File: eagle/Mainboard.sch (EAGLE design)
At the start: 31 parts, among them IC1 L293D, IC2 TLC272P, IC3 LM1085IT-5.0

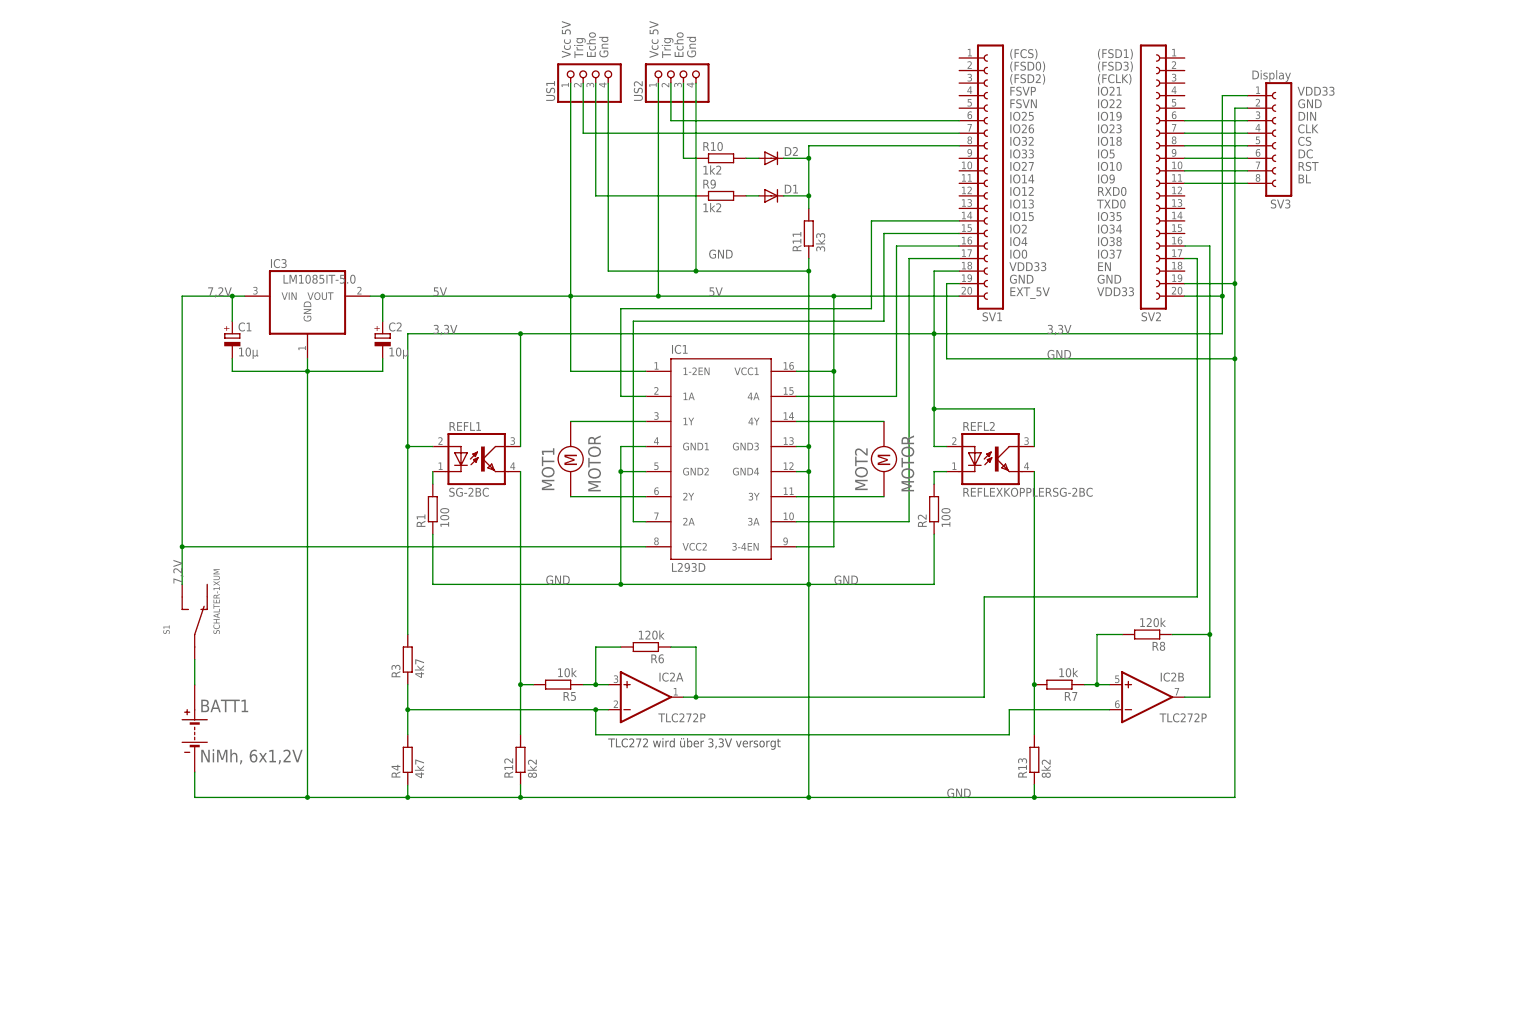
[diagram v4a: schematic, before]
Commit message: Messung Akkuspannung hinzugefügt. SPI-Pins verschoben, damit sie mit SPI3 zusammenpassen
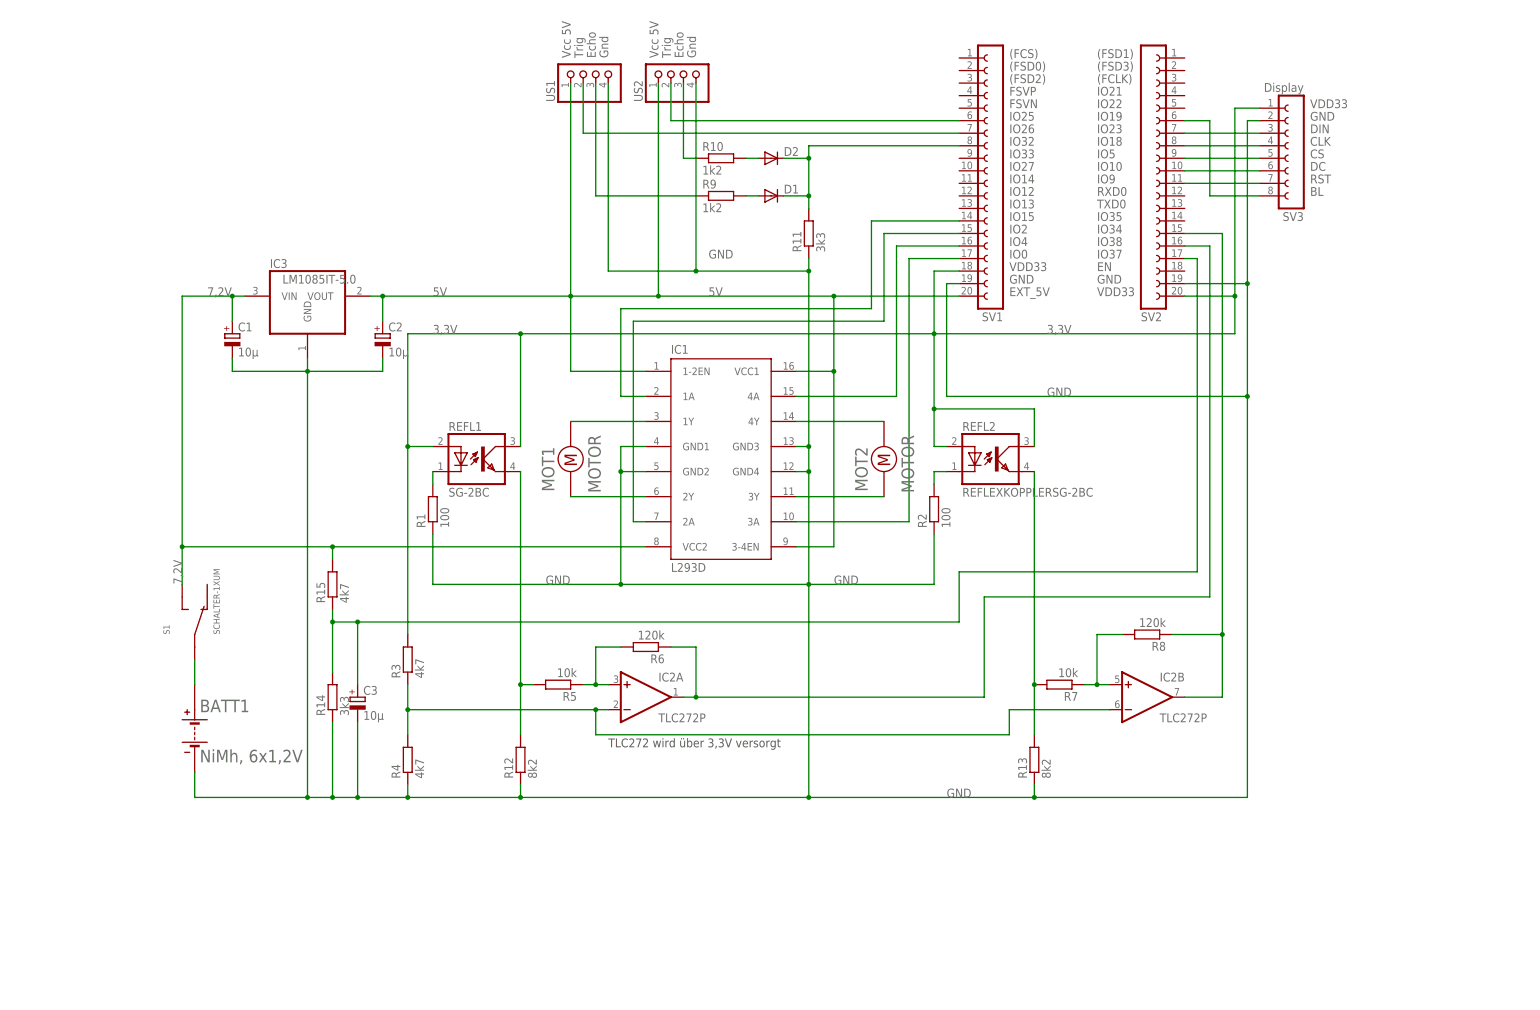
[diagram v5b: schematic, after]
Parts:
- added C3: 10µ, rcl:CPOL-EUE3.5-10
- added R14: 3k3, rcl:R-EU_RDH/15
- added R15: 4k7, rcl:R-EU_RDH/15
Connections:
- removed net N$27: SV2.11, SV3.8
- new net N$20: SV2.6, SV3.8
- new net N$25: C3.+, R14.2, R15.1, SV2.17
- net 7,2V: now also R15.2
- net GND: now also C3.-, R14.1
- net N$11: now also SV2.8; no longer SV2.7
- net N$16: now also SV2.9; no longer SV2.8
- net N$17: now also SV2.10; no longer SV2.9
- net N$18: now also SV2.11; no longer SV2.10
- net N$21: now also SV2.16; no longer SV2.17
- net N$28: now also SV2.15; no longer SV2.16
- net N$8: now also SV2.7; no longer SV2.6
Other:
- moved on the sheet: SV3

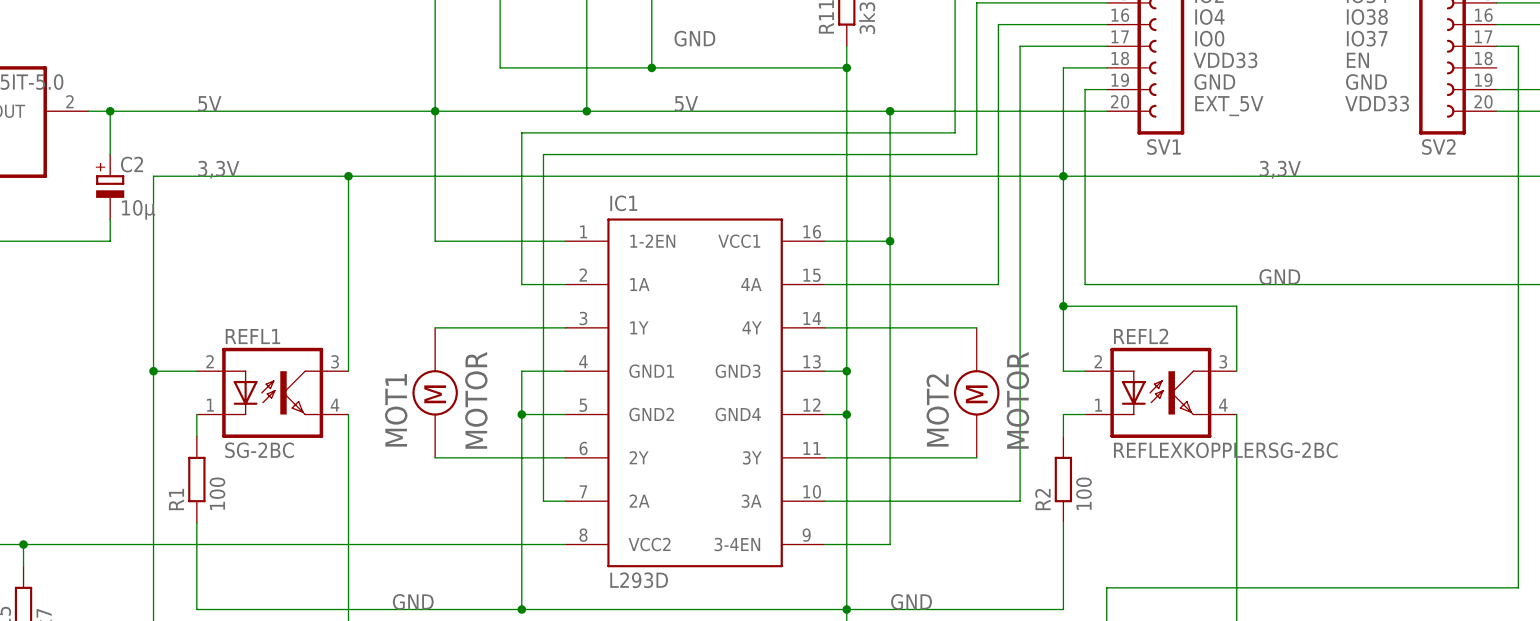
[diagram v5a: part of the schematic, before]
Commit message: Sketch für Mainboard hinzugefügt
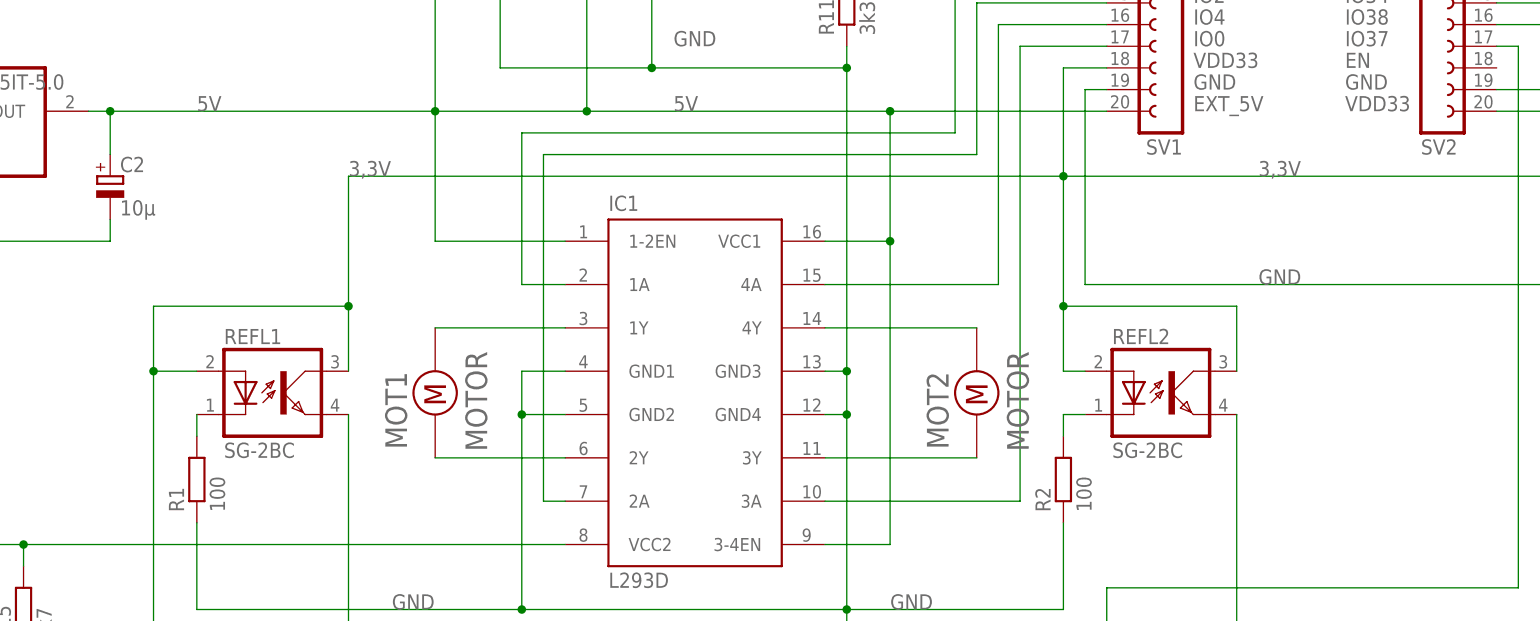
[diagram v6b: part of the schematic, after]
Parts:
- REFL2: value REFLEXKOPPLERSG-2BC -> SG-2BC
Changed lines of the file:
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@@
 <part name="IC1" library="st-microelectronics" library_urn="urn:adsk.eagle:library:368" deviceset="L293D" device="" package3d_urn="urn:adsk.eagle:package:26820/1"/>
 <part name="REFL1" library="bs_lib" deviceset="REFLEXKOPPLER" device="SG-2BC" value="SG-2BC"/>
-<part name="REFL2" library="bs_lib" deviceset="REFLEXKOPPLER" device="SG-2BC"/>
+<part name="REFL2" library="bs_lib" deviceset="REFLEXKOPPLER" device="SG-2BC" value="SG-2BC"/>
 <part name="IC2" library="linear" library_urn="urn:adsk.eagle:library:262" deviceset="TLC272" device="P" package3d_urn="urn:adsk.eagle:package:16409/2"/>
 <part name="MOT1" library="bs_lib" deviceset="MOTOR" device=""/>
@@
 <wire x1="208.28" y1="106.68" x2="198.12" y2="106.68" width="0.1524" layer="91"/>
 <pinref part="REFL1" gate="G$1" pin="COL"/>
-<wire x1="63.5" y1="99.06" x2="63.5" y2="76.2" width="0.1524" layer="91"/>
-<wire x1="40.64" y1="99.06" x2="63.5" y2="99.06" width="0.1524" layer="91"/>
+<wire x1="63.5" y1="99.06" x2="63.5" y2="83.82" width="0.1524" layer="91"/>
+<wire x1="63.5" y1="83.82" x2="63.5" y2="76.2" width="0.1524" layer="91"/>
 <wire x1="147.32" y1="99.06" x2="63.5" y2="99.06" width="0.1524" layer="91"/>
 <junction x="147.32" y="99.06"/>
-<junction x="63.5" y="99.06"/>
 <pinref part="REFL2" gate="G$1" pin="A"/>
 <wire x1="149.86" y1="76.2" x2="147.32" y2="76.2" width="0.1524" layer="91"/>
@@
 <pinref part="SV3" gate="G$1" pin="1"/>
 <wire x1="208.28" y1="144.78" x2="213.36" y2="144.78" width="0.1524" layer="91"/>
-<label x="45.72" y="99.06" size="1.778" layer="95"/>
+<label x="63.5" y="99.06" size="1.778" layer="95"/>
 <pinref part="R3" gate="G$1" pin="2"/>
 <pinref part="REFL1" gate="G$1" pin="A"/>
 <wire x1="45.72" y1="76.2" x2="40.64" y2="76.2" width="0.1524" layer="91"/>
 <wire x1="40.64" y1="76.2" x2="40.64" y2="38.1" width="0.1524" layer="91"/>
-<wire x1="40.64" y1="99.06" x2="40.64" y2="76.2" width="0.1524" layer="91"/>
 <junction x="40.64" y="76.2"/>
-</segment>
-</net>
+<wire x1="40.64" y1="83.82" x2="40.64" y2="76.2" width="0.1524" layer="91"/>
+<wire x1="40.64" y1="83.82" x2="63.5" y2="83.82" width="0.1524" layer="91"/>
+<junction x="63.5" y="83.82"/>
+</segment>
+</net>
